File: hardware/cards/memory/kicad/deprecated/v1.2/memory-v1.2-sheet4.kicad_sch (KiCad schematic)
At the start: 5 parts, among them IC11 74*157, IC8 74*244, IC9 74*244

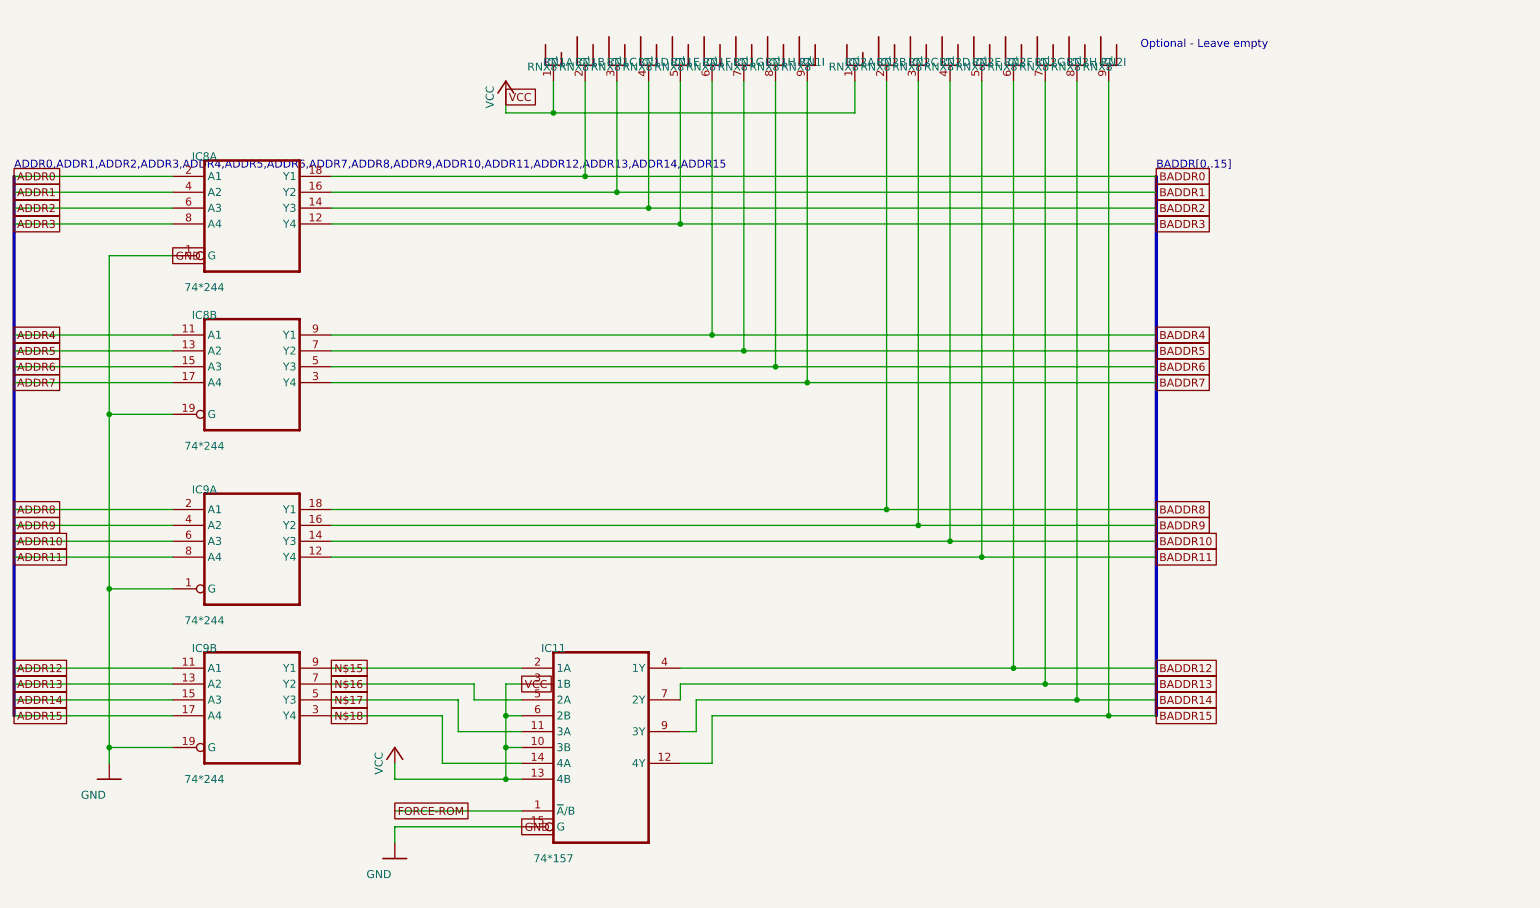
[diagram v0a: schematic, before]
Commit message: fix(kicad): readable converted schematics - overlaps 42,847 -> 3,147, nothing off the frame; CF sheet 0 overlaps
- tools/kicad/sch_overlaps.py: calibrated readability check (text/text, text/body, text/line, off frame/title block)
- eagle_sch_to_kicad.py: fields placed from Eagle's smashed attributes or the symbol's >NAME/>VALUE with Eagle's align,
  size and ratio, readable angles; fields Eagle never shows hidden (FABC96R shows only its pin name); pin numbers hidden
  where every Eagle pin hides them; Eagle-hidden layers dropped (the stray SpiceOrder text); labels on their own wires,
  converter labels only where KiCad needs them; rotate-then-mirror fixed for MR90/MR270 in pin_world/no-connects;
  each sheet on the smallest page that holds it, centred clear of the title block
- finish_board.py: stable footprint-library choice (DRC counts no longer vary run to run)
- all 37 projects regenerated: netlist proofs unchanged (34 MATCH, 2 schematic-only, video Fusion export MISMATCH as
  before); DRC same or better; ERC up (loose wire ends onto graphic buses no longer hidden by labels; explained per README)
- CF card: gate names off the gate bodies, U3 clear of its title, 5.08 mm connector pins; rebuilt: DRC 0/0, proof MATCH
- schematic PDFs regenerated (tools/sch_to_pdf.py, 37/37)

Co-Authored-By: Claude Opus 5.5 <noreply@anthropic.com>
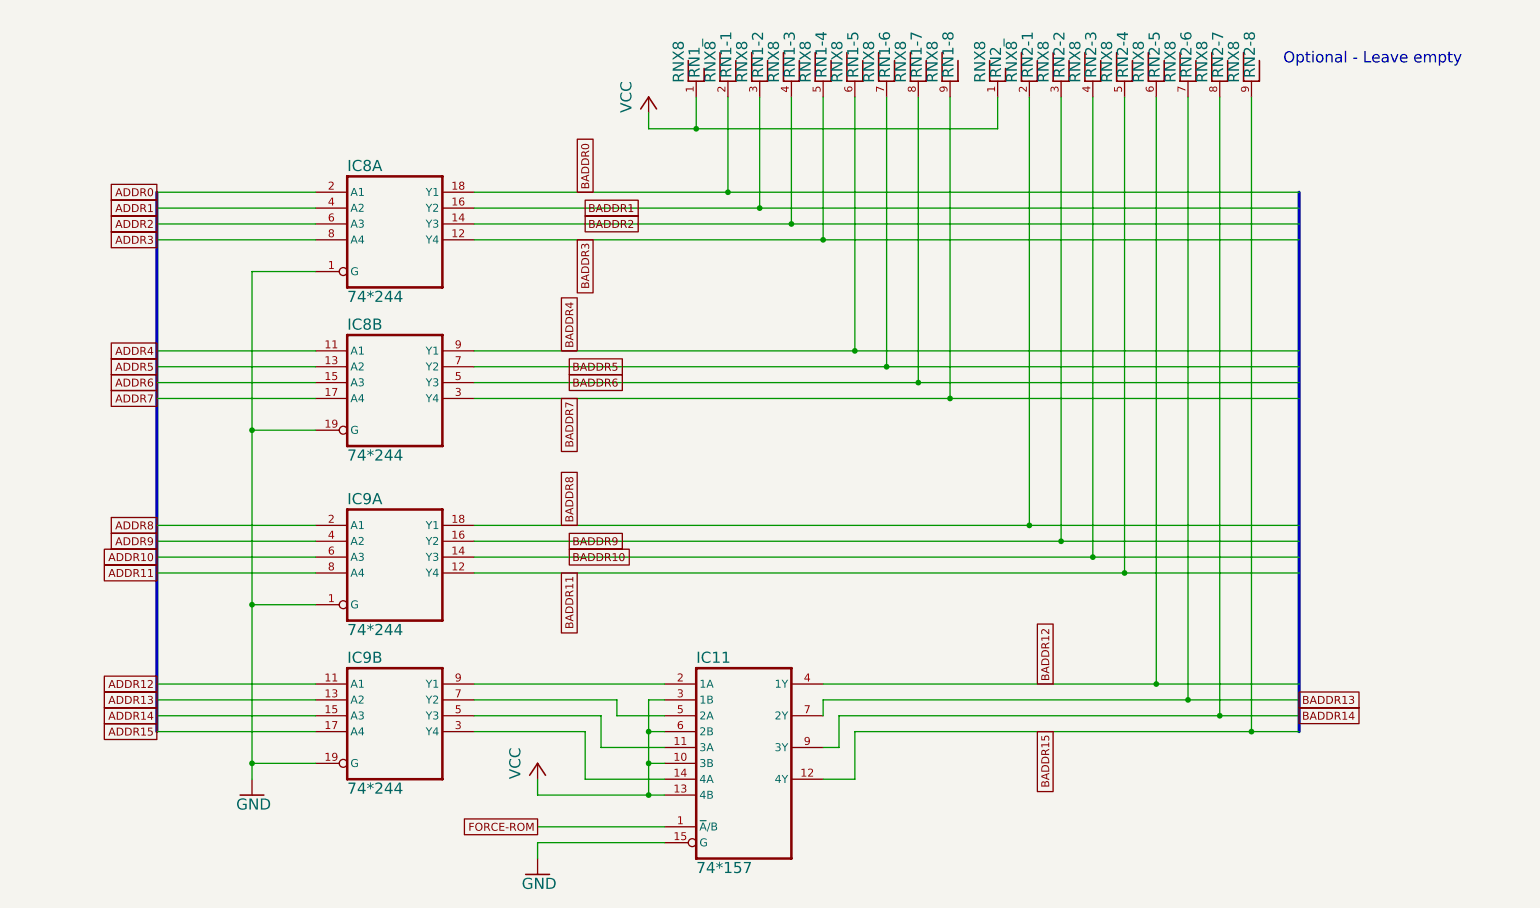
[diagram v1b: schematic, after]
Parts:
- RN1: Eagle name (none) -> RN1-3
- RN1: Eagle name (none) -> RN1-8
- RN1: Eagle name (none) -> RN1-5
- RN1: Eagle name (none) -> RN1-2
- RN1: Eagle name (none) -> RN1-1
- RN1: Eagle name (none) -> RN1-7
- RN1: Eagle name (none) -> RN1_
- RN1: Eagle name (none) -> RN1-4
- RN1: Eagle name (none) -> RN1-6
- RN2: Eagle name (none) -> RN2_
- RN2: Eagle name (none) -> RN2-8
- RN2: Eagle name (none) -> RN2-7
- RN2: Eagle name (none) -> RN2-1
- RN2: Eagle name (none) -> RN2-2
- RN2: Eagle name (none) -> RN2-3
- RN2: Eagle name (none) -> RN2-4
- RN2: Eagle name (none) -> RN2-6
- RN2: Eagle name (none) -> RN2-5
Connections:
- net N$15: no longer names the net of IC11.2 (1A), IC9.9 (Y1)
- net N$16: no longer names the net of IC11.5 (2A), IC9.7 (Y2)
- net N$17: no longer names the net of IC11.11 (3A), IC9.5 (Y3)
- net N$18: no longer names the net of IC11.14 (4A), IC9.3 (Y4)
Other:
- note removed: "ADDR0,ADDR1,ADDR2,ADDR3,ADDR4,ADDR5,ADDR6,ADDR7,ADDR8,ADDR9,ADDR10,ADDR11,ADDR12,ADDR13,ADDR14,ADDR15"
- note removed: "BADDR[0..15]"
- moved on the sheet: IC11, IC8A, IC8B, IC9A, IC9B
